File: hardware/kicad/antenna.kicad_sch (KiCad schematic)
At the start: 11 parts, among them J5 BWIPX-1-001E

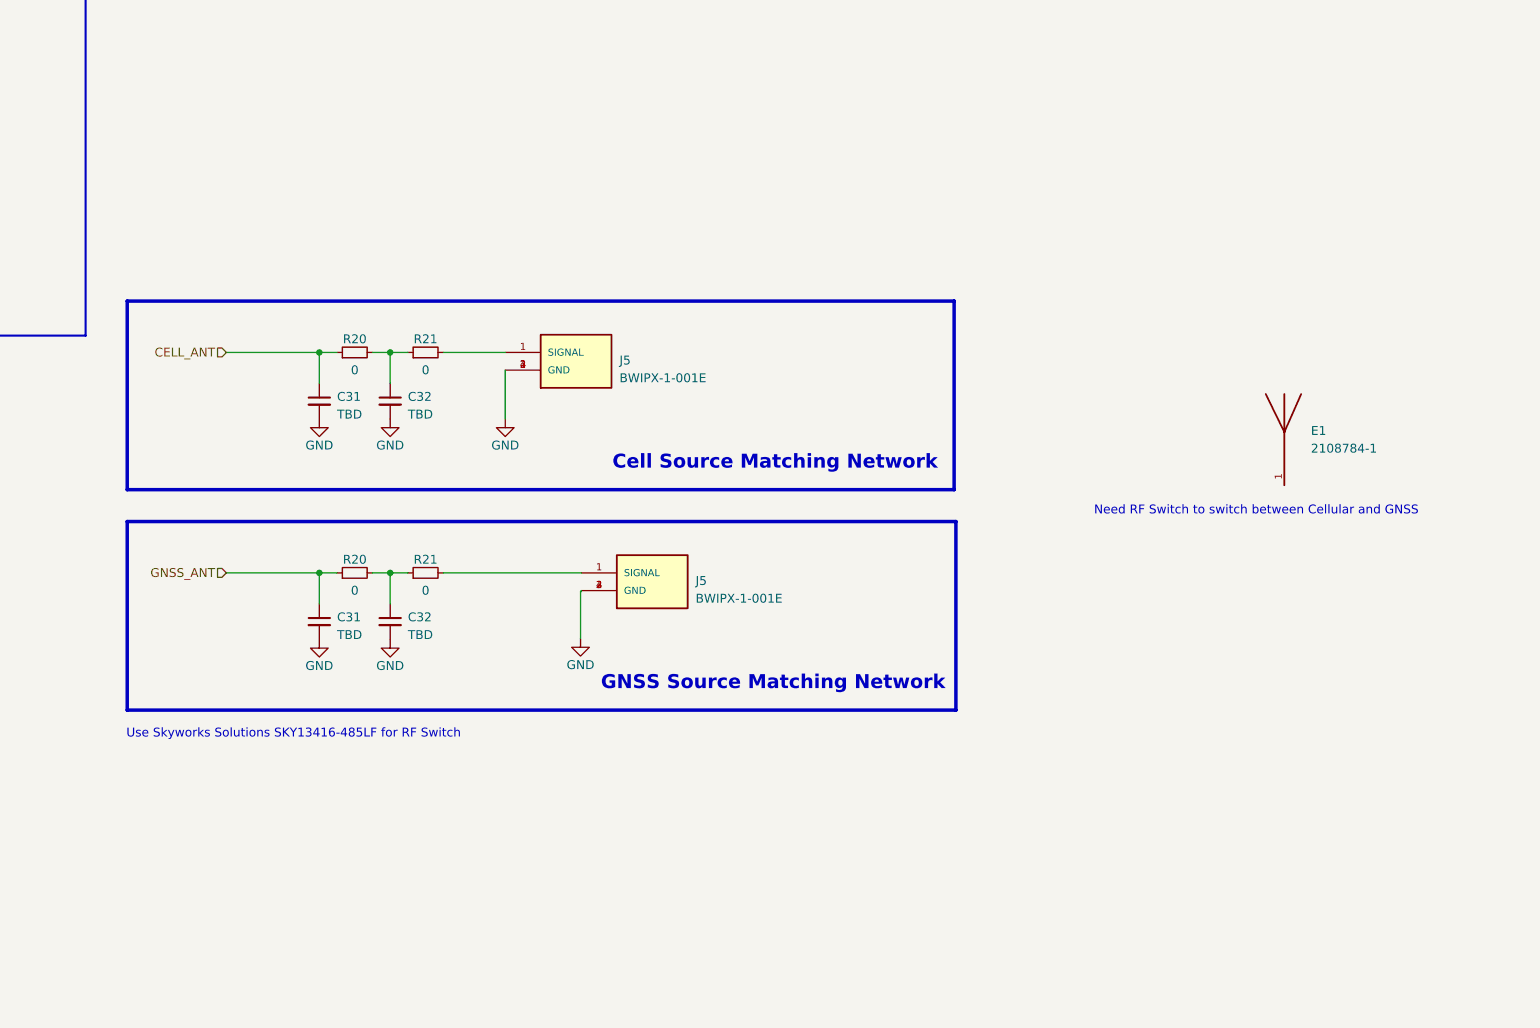
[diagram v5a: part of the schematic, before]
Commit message: update antenna schematic
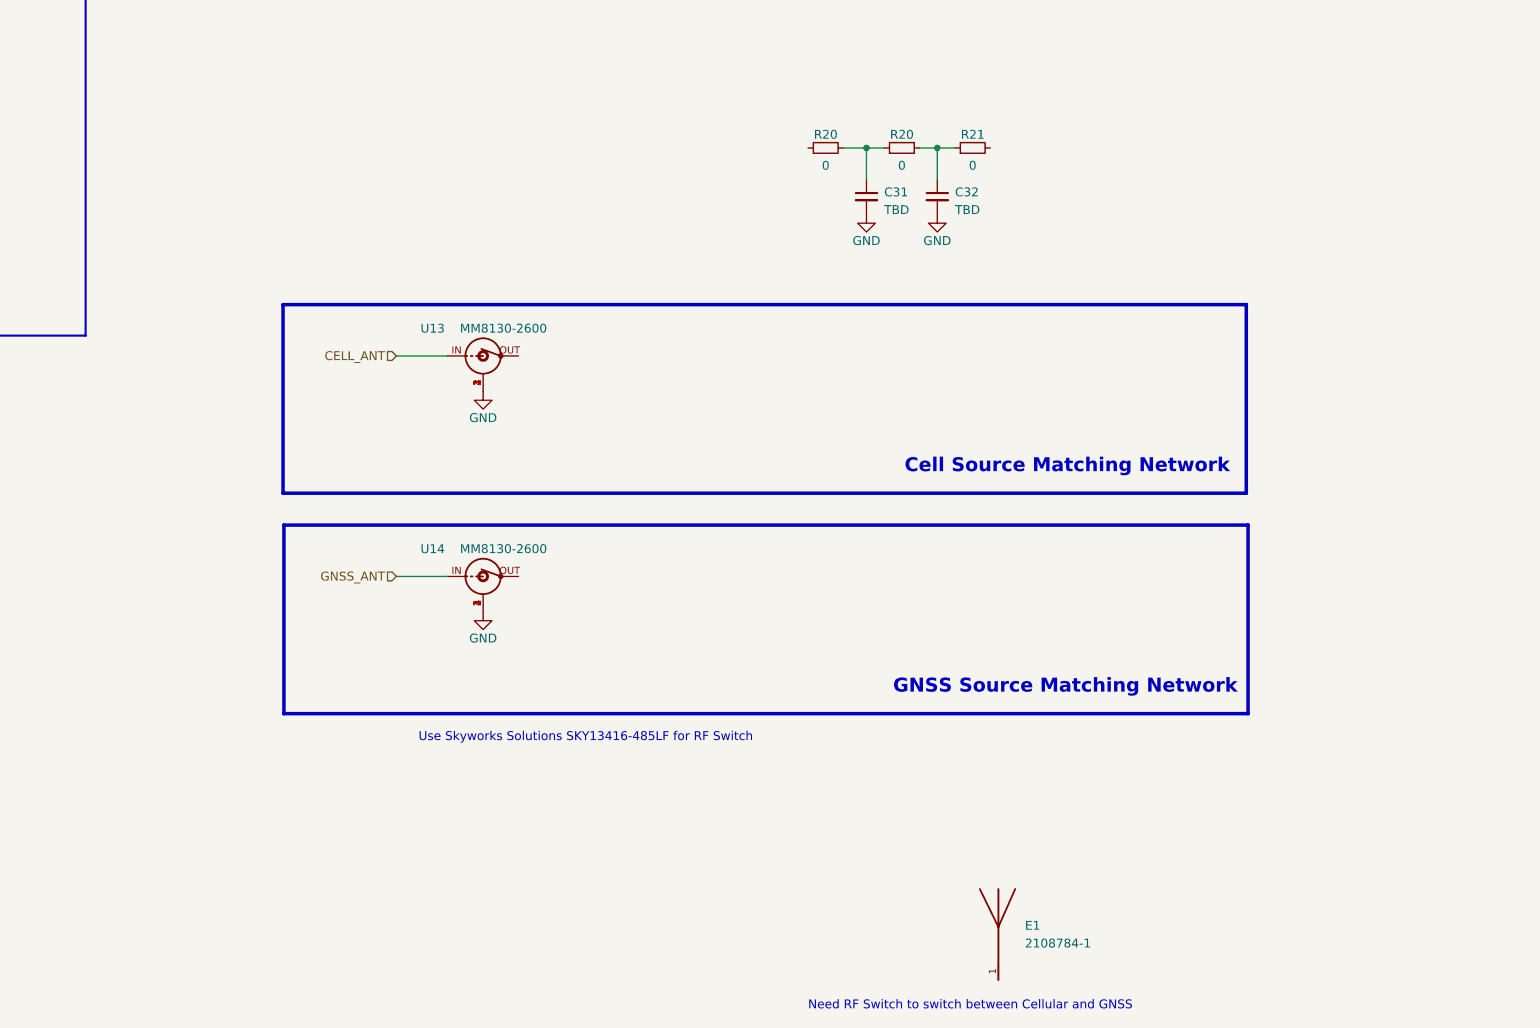
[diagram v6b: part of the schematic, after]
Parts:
- removed C31 (x2), C32 (x2): TBD, Capacitor_SMD:C_0402_1005Metric, symbol Device:C_Small
- removed J5 (x2): BWIPX-1-001E, SAMTEC_RSP-122811-02:SAMTEC_RSP-122811-02, symbol RSP-122811-02:RSP-122811-02
- removed R20 (x2), R21 (x2): 0, Resistor_SMD:R_0402_1005Metric, symbol Device:R_Small
- added C31, C32: TBD, Capacitor_SMD:C_0402_1005Metric, symbol Device:C_Small
- added R20 (x2), R21: 0, Resistor_SMD:R_0402_1005Metric, symbol Device:R_Small
- added U13, U14: MM8130-2600, bwlc1a:MM8130-2600, symbol bwlc1a:MM8130-2600
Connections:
- net CELL_ANT: now also U13.IN
- net GND: now also C31.2, C32.2, U13.1, U13.2, U13.3, U13.4, U14.1, U14.2, U14.3, U14.4
- net GNSS_ANT: now also U14.IN
- new net: C32.1, R20.2, R21.1
- new net: C31.1, R20.1, R20.2
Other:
- moved on the sheet: E1

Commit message: update antenna
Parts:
- added U15, U16: SKY13414-485LF, symbol bwlc1a:SKY13414-485LF
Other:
- moved on the sheet: E1
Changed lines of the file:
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@@
 (kicad_sch (version 20230121) (generator eeschema)
-  (paper "A4")
+  (paper "A3")
   (junction (at 204.216 38.608) (diameter 0) (color 0 0 0 0)
   )
@@
     )
   )
-  (symbol (lib_id "bwlc1a:2108784-1") (at 212.979 152.908 0) (unit 1)
+  (symbol (lib_id "bwlc1a:2108784-1") (at 391.414 87.884 0) (unit 1)
     (in_bom yes) (on_board yes) (dnp no) (fields_autoplaced)
-    (property "Reference" "E1" (at 216.789 150.1775 0)
+    (property "Reference" "E1" (at 395.224 85.1535 0)
       (effects (font (size 1.27 1.27)) (justify left))
     )
-    (property "Value" "2108784-1" (at 216.789 152.7175 0)
+    (property "Value" "2108784-1" (at 395.224 87.6935 0)
       (effects (font (size 1.27 1.27)) (justify left))
     )
-    (property "Footprint" "bwlc1a:2108784-1" (at 212.979 152.908 0)
+    (property "Footprint" "bwlc1a:2108784-1" (at 391.414 87.884 0)
       (effects (font (size 1.27 1.27)) (justify bottom) hide)
     )
-    (property "Datasheet" "" (at 212.979 152.908 0)
+    (property "Datasheet" "" (at 391.414 87.884 0)
       (effects (font (size 1.27 1.27)) hide)
     )
@@
         (path "/388039b1-99cc-430f-bd4a-010573fde798/ca79f09e-abdb-462a-9aab-98f2e37e5b23"
           (reference "#PWR026") (unit 1)
+        )
+      )
+    )
+  )
+  (symbol (lib_id "bwlc1a:SKY13414-485LF") (at 344.424 95.758 0) (unit 1)
+    (in_bom yes) (on_board yes) (dnp no) (fields_autoplaced)
+    (property "Reference" "U16" (at 344.424 75.819 0)
+      (effects (font (size 1.27 1.27)))
+    )
+    (property "Value" "SKY13414-485LF" (at 344.424 78.359 0)
+      (effects (font (size 1.27 1.27)))
+    )
+    (property "Footprint" "" (at 344.424 116.078 0)
+      (effects (font (size 1.27 1.27)) (justify bottom) hide)
+    )
+    (property "Datasheet" "" (at 344.424 95.758 0)
+      (effects (font (size 1.27 1.27)) hide)
+    )
+    (pin "1")
+    (pin "10")
+    (pin "11")
+    (pin "12")
+    (pin "13")
+    (pin "14")
+    (pin "15")
+    (pin "2")
+    (pin "3")
+    (pin "4")
+    (pin "5")
+    (pin "6")
+    (pin "7")
+    (pin "8")
+    (pin "9")
+    (instances
+      (project "bwlc1a"
+        (path "/388039b1-99cc-430f-bd4a-010573fde798/ca79f09e-abdb-462a-9aab-98f2e37e5b23"
+          (reference "U16") (unit 1)
         )
       )
@@
         )
       )
+    )
+  )
+  (symbol (lib_id "bwlc1a:SKY13414-485LF") (at 292.608 95.758 0) (mirror y) (unit 1)
+    (in_bom yes) (on_board yes) (dnp no)
+    (property "Reference" "U15" (at 292.608 75.819 0)
+      (effects (font (size 1.27 1.27)))
+    )
+    (property "Value" "SKY13414-485LF" (at 292.608 78.359 0)
+      (effects (font (size 1.27 1.27)))
+    )
+    (property "Footprint" "" (at 292.608 116.078 0)
+      (effects (font (size 1.27 1.27)) (justify bottom) hide)
+    )
+    (property "Datasheet" "" (at 292.608 95.758 0)
+      (effects (font (size 1.27 1.27)) hide)
+    )
+    (pin "1")
+    (pin "10")
+    (pin "11")
+    (pin "12")
+    (pin "13")
+    (pin "14")
+    (pin "15")
+    (pin "2")
+    (pin "3")
+    (pin "4")
+    (pin "5")
+    (pin "6")
+    (pin "7")
+    (pin "8")
+    (pin "9")
+    (instances
+      (project "bwlc1a"
+        (path "/388039b1-99cc-430f-bd4a-010573fde798/ca79f09e-abdb-462a-9aab-98f2e37e5b23"
+          (reference "U15") (unit 1)
+        )
+      )

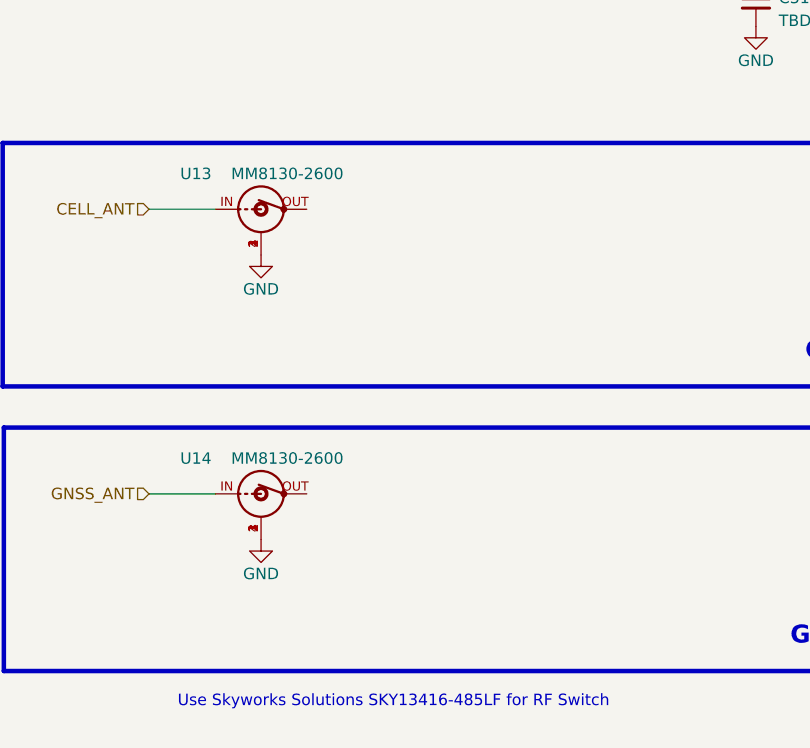
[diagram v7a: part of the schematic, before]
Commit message: add test point for on-board antenna
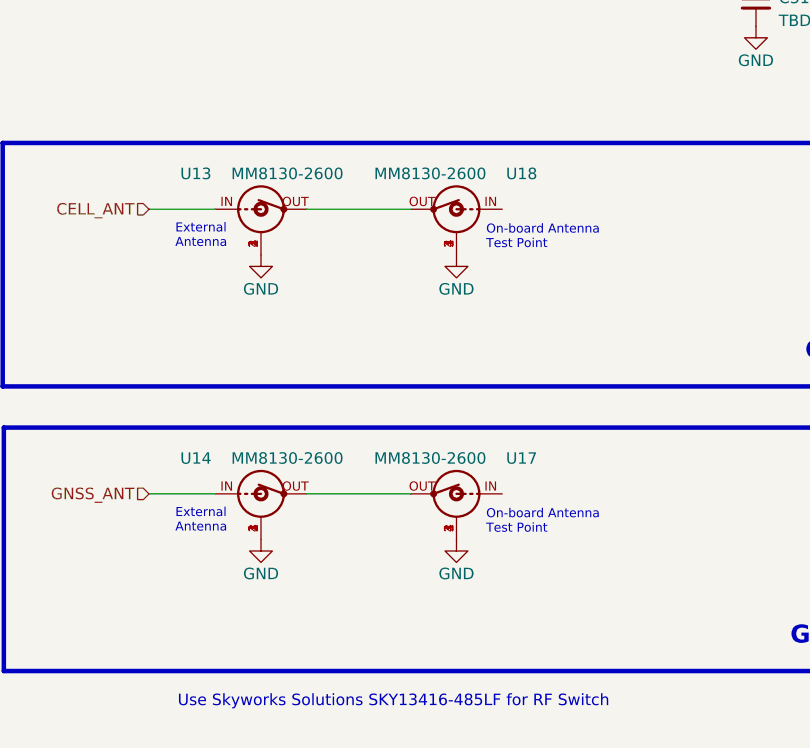
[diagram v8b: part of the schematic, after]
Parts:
- added U17, U18: MM8130-2600, bwlc1a:MM8130-2600, symbol bwlc1a:MM8130-2600
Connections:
- net GND: now also U17.1, U17.2, U17.3, U17.4, U18.1, U18.2, U18.3, U18.4
- net at U14.OUT: now also U17.OUT
- net at U13.OUT: now also U18.OUT
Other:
- note added: "External Antenna"
- note added: "On-board Antenna Test Point"
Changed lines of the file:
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@@
   (junction (at 194.056 38.608) (diameter 0) (color 0 0 0 0)
   )
+  (wire (pts (xy 144.145 100.076) (xy 155.702 100.076))
+    (stroke (width 0) (type default))
+  )
   (wire (pts (xy 126.619 100.076) (xy 133.985 100.076))
     (stroke (width 0) (type default))
   )
   (wire (pts (xy 204.216 38.608) (xy 204.216 43.053))
+    (stroke (width 0) (type default))
+  )
+  (wire (pts (xy 144.145 68.453) (xy 155.702 68.453))
     (stroke (width 0) (type default))
   )
@@
     (effects (font (size 2 2) (thickness 0.6) bold) (justify left bottom))
   )
+  (text "External \nAntenna" (at 129.54 104.521 0)
+    (effects (font (size 1 1)) (justify left bottom))
+  )
   (text "A7670C Frequency" (at 36.957 20.828 0)
     (effects (font (size 2 2) (thickness 0.4) bold) (justify left bottom))
+  )
+  (text "External \nAntenna" (at 129.54 72.898 0)
+    (effects (font (size 1 1)) (justify left bottom))
   )
   (text "Need RF Switch to switch between Cellular and GNSS"
     (at 185.674 162.433 0)
     (effects (font (size 1.27 1.27)) (justify left bottom))
+  )
+  (text "On-board Antenna\nTest Point" (at 164.084 104.648 0)
+    (effects (font (size 1 1)) (justify left bottom))
+  )
+  (text "On-board Antenna\nTest Point" (at 164.084 73.025 0)
+    (effects (font (size 1 1)) (justify left bottom))
   )
   (text "* common antenna range :\n	824MHz~960MHz\n	1710MHz~2170MHz \n	1710MHz~2690MHz"
@@
     )
   )
+  (symbol (lib_id "power:GND") (at 160.782 105.156 0) (unit 1)
+    (in_bom yes) (on_board yes) (dnp no)
+    (property "Reference" "#PWR041" (at 160.782 111.506 0)
+      (effects (font (size 1.27 1.27)) hide)
+    )
+    (property "Value" "GND" (at 160.782 108.966 0)
+      (effects (font (size 1.27 1.27)))
+    )
+    (property "Footprint" "" (at 160.782 105.156 0)
+      (effects (font (size 1.27 1.27)) hide)
+    )
+    (property "Datasheet" "" (at 160.782 105.156 0)
+      (effects (font (size 1.27 1.27)) hide)
+    )
+    (pin "1")
+    (instances
+      (project "bwlc1a"
+        (path "/388039b1-99cc-430f-bd4a-010573fde798"
+          (reference "#PWR041") (unit 1)
+        )
+        (path "/388039b1-99cc-430f-bd4a-010573fde798/d0b0fe7e-ffcb-4a20-b7b5-70f0caeaf6a1"
+          (reference "#PWR080") (unit 1)
+        )
+        (path "/388039b1-99cc-430f-bd4a-010573fde798/ca79f09e-abdb-462a-9aab-98f2e37e5b23"
+          (reference "#PWR019") (unit 1)
+        )
+      )
+    )
+  )
   (symbol (lib_id "Device:R_Small") (at 188.214 38.608 90) (unit 1)
     (in_bom yes) (on_board yes) (dnp no)
@@
         )
         (path "/388039b1-99cc-430f-bd4a-010573fde798/ca79f09e-abdb-462a-9aab-98f2e37e5b23"
-          (reference "#PWR026") (unit 1)
+          (reference "#PWR020") (unit 1)
         )
       )
@@
     )
   )
+  (symbol (lib_id "bwlc1a:MM8130-2600") (at 160.782 100.076 0) (mirror y) (unit 1)
+    (in_bom yes) (on_board yes) (dnp no)
+    (property "Reference" "U17" (at 168.021 96.139 0)
+      (effects (font (size 1.27 1.27)))
+    )
+    (property "Value" "MM8130-2600" (at 157.861 96.139 0)
+      (effects (font (size 1.27 1.27)))
+    )
+    (property "Footprint" "bwlc1a:MM8130-2600" (at 160.782 114.046 0)
+      (effects (font (size 1.27 1.27)) (justify bottom) hide)
+    )
+    (property "Datasheet" "" (at 160.782 100.076 0)
+      (effects (font (size 1.27 1.27)) hide)
+    )
+    (pin "1")
+    (pin "2")
+    (pin "3")
+    (pin "4")
+    (pin "IN")
+    (pin "OUT")
+    (instances
+      (project "bwlc1a"
+        (path "/388039b1-99cc-430f-bd4a-010573fde798/ca79f09e-abdb-462a-9aab-98f2e37e5b23"
+          (reference "U17") (unit 1)
+        )
+      )
+    )
+  )
   (symbol (lib_id "Device:C_Small") (at 194.056 45.593 0) (unit 1)
     (in_bom yes) (on_board yes) (dnp no) (fields_autoplaced)
@@
         )
       )
+    )
+  )
+  (symbol (lib_id "bwlc1a:MM8130-2600") (at 160.782 68.453 0) (mirror y) (unit 1)
+    (in_bom yes) (on_board yes) (dnp no)
+    (property "Reference" "U18" (at 168.021 64.516 0)
+      (effects (font (size 1.27 1.27)))
+    )
+    (property "Value" "MM8130-2600" (at 157.861 64.516 0)
+      (effects (font (size 1.27 1.27)))
+    )
+    (property "Footprint" "bwlc1a:MM8130-2600" (at 160.782 82.423 0)
+      (effects (font (size 1.27 1.27)) (justify bottom) hide)
+    )
+    (property "Datasheet" "" (at 160.782 68.453 0)
+      (effects (font (size 1.27 1.27)) hide)
+    )
+    (pin "1")
+    (pin "2")
+    (pin "3")
+    (pin "4")
+    (pin "IN")
+    (pin "OUT")
+    (instances
+      (project "bwlc1a"
+        (path "/388039b1-99cc-430f-bd4a-010573fde798/ca79f09e-abdb-462a-9aab-98f2e37e5b23"
+          (reference "U18") (unit 1)
+        )
+      )
+    )
+  )
+  (symbol (lib_id "power:GND") (at 160.782 73.533 0) (unit 1)
+    (in_bom yes) (on_board yes) (dnp no)
+    (property "Reference" "#PWR041" (at 160.782 79.883 0)
+      (effects (font (size 1.27 1.27)) hide)
+    )
+    (property "Value" "GND" (at 160.782 77.343 0)
+      (effects (font (size 1.27 1.27)))
+    )
+    (property "Footprint" "" (at 160.782 73.533 0)
+      (effects (font (size 1.27 1.27)) hide)
+    )
+    (property "Datasheet" "" (at 160.782 73.533 0)
+      (effects (font (size 1.27 1.27)) hide)
+    )
+    (pin "1")
+    (instances
+      (project "bwlc1a"
+        (path "/388039b1-99cc-430f-bd4a-010573fde798"
+          (reference "#PWR041") (unit 1)
+        )
+        (path "/388039b1-99cc-430f-bd4a-010573fde798/d0b0fe7e-ffcb-4a20-b7b5-70f0caeaf6a1"
+          (reference "#PWR080") (unit 1)
+        )
+        (path "/388039b1-99cc-430f-bd4a-010573fde798/ca79f09e-abdb-462a-9aab-98f2e37e5b23"
+          (reference "#PWR026") (unit 1)
+        )
+      )
